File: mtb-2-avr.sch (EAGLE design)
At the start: 15 parts, among them IC1 MEGA328P-AU, Q1 14.745 MHz

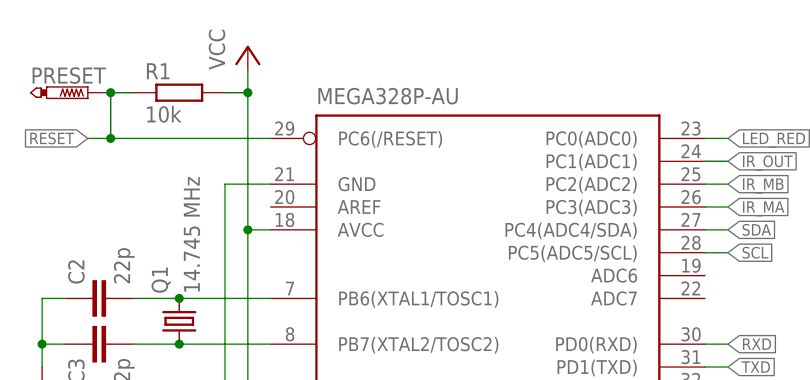
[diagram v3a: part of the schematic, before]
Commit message: Use ATmega8A, fix silksreen.
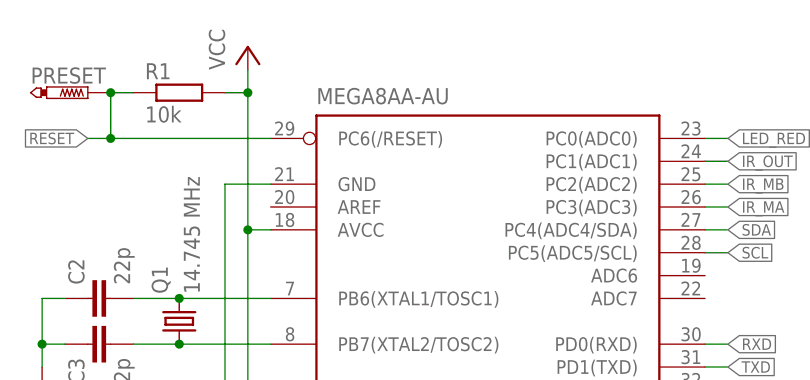
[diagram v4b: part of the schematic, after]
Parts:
- IC1: value MEGA328P-AU -> MEGA8AA-AU; LCSC_PART C14877 -> C16190
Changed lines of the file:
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@@
 <grid distance="0.1" unitdist="inch" unit="mm" style="lines" multiple="1" display="no" altdistance="0.01" altunitdist="inch" altunit="mm"/>
 <layers>
-<layer number="1" name="Top" color="3" fill="1" visible="yes" active="no"/>
-<layer number="2" name="Route2" color="16" fill="1" visible="yes" active="no"/>
-<layer number="3" name="Route3" color="17" fill="1" visible="yes" active="no"/>
-<layer number="4" name="Route4" color="18" fill="1" visible="yes" active="no"/>
-<layer number="5" name="Route5" color="19" fill="1" visible="yes" active="no"/>
-<layer number="6" name="Route6" color="25" fill="1" visible="yes" active="no"/>
-<layer number="7" name="Route7" color="26" fill="1" visible="yes" active="no"/>
-<layer number="8" name="Route8" color="27" fill="1" visible="yes" active="no"/>
-<layer number="9" name="Route9" color="28" fill="1" visible="yes" active="no"/>
-<layer number="10" name="Route10" color="29" fill="1" visible="yes" active="no"/>
-<layer number="11" name="Route11" color="30" fill="1" visible="yes" active="no"/>
-<layer number="12" name="Route12" color="20" fill="1" visible="yes" active="no"/>
-<layer number="13" name="Route13" color="21" fill="1" visible="yes" active="no"/>
-<layer number="14" name="Route14" color="22" fill="1" visible="yes" active="no"/>
-<layer number="15" name="Route15" color="23" fill="1" visible="yes" active="no"/>
-<layer number="16" name="Bottom" color="4" fill="1" visible="yes" active="no"/>
-<layer number="17" name="Pads" color="2" fill="1" visible="yes" active="no"/>
-<layer number="18" name="Vias" color="2" fill="1" visible="yes" active="no"/>
-<layer number="19" name="Unrouted" color="6" fill="1" visible="yes" active="no"/>
-<layer number="20" name="Dimension" color="24" fill="1" visible="yes" active="no"/>
-<layer number="21" name="tPlace" color="7" fill="1" visible="yes" active="no"/>
-<layer number="22" name="bPlace" color="7" fill="1" visible="yes" active="no"/>
-<layer number="23" name="tOrigins" color="15" fill="1" visible="yes" active="no"/>
-<layer number="24" name="bOrigins" color="15" fill="1" visible="yes" active="no"/>
-<layer number="25" name="tNames" color="7" fill="1" visible="yes" active="no"/>
-<layer number="26" name="bNames" color="7" fill="1" visible="yes" active="no"/>
-<layer number="27" name="tValues" color="7" fill="1" visible="yes" active="no"/>
-<layer number="28" name="bValues" color="7" fill="1" visible="yes" active="no"/>
+<layer number="1" name="Top" color="3" fill="1" visible="no" active="no"/>
+<layer number="2" name="Route2" color="16" fill="1" visible="no" active="no"/>
+<layer number="3" name="Route3" color="17" fill="1" visible="no" active="no"/>
+<layer number="4" name="Route4" color="18" fill="1" visible="no" active="no"/>
+<layer number="5" name="Route5" color="19" fill="1" visible="no" active="no"/>
+<layer number="6" name="Route6" color="25" fill="1" visible="no" active="no"/>
+<layer number="7" name="Route7" color="26" fill="1" visible="no" active="no"/>
+<layer number="8" name="Route8" color="27" fill="1" visible="no" active="no"/>
+<layer number="9" name="Route9" color="28" fill="1" visible="no" active="no"/>
+<layer number="10" name="Route10" color="29" fill="1" visible="no" active="no"/>
+<layer number="11" name="Route11" color="30" fill="1" visible="no" active="no"/>
+<layer number="12" name="Route12" color="20" fill="1" visible="no" active="no"/>
+<layer number="13" name="Route13" color="21" fill="1" visible="no" active="no"/>
+<layer number="14" name="Route14" color="22" fill="1" visible="no" active="no"/>
+<layer number="15" name="Route15" color="23" fill="1" visible="no" active="no"/>
+<layer number="16" name="Bottom" color="4" fill="1" visible="no" active="no"/>
+<layer number="17" name="Pads" color="2" fill="1" visible="no" active="no"/>
+<layer number="18" name="Vias" color="2" fill="1" visible="no" active="no"/>
+<layer number="19" name="Unrouted" color="6" fill="1" visible="no" active="no"/>
+<layer number="20" name="Dimension" color="24" fill="1" visible="no" active="no"/>
+<layer number="21" name="tPlace" color="7" fill="1" visible="no" active="no"/>
+<layer number="22" name="bPlace" color="7" fill="1" visible="no" active="no"/>
+<layer number="23" name="tOrigins" color="15" fill="1" visible="no" active="no"/>
+<layer number="24" name="bOrigins" color="15" fill="1" visible="no" active="no"/>
+<layer number="25" name="tNames" color="7" fill="1" visible="no" active="no"/>
+<layer number="26" name="bNames" color="7" fill="1" visible="no" active="no"/>
+<layer number="27" name="tValues" color="7" fill="1" visible="no" active="no"/>
+<layer number="28" name="bValues" color="7" fill="1" visible="no" active="no"/>
 <layer number="29" name="tStop" color="7" fill="3" visible="no" active="no"/>
 <layer number="30" name="bStop" color="7" fill="6" visible="no" active="no"/>
@@
 <layer number="35" name="tGlue" color="7" fill="4" visible="no" active="no"/>
 <layer number="36" name="bGlue" color="7" fill="5" visible="no" active="no"/>
-<layer number="37" name="tTest" color="7" fill="1" visible="yes" active="no"/>
-<layer number="38" name="bTest" color="7" fill="1" visible="yes" active="no"/>
+<layer number="37" name="tTest" color="7" fill="1" visible="no" active="no"/>
+<layer number="38" name="bTest" color="7" fill="1" visible="no" active="no"/>
 <layer number="39" name="tKeepout" color="4" fill="11" visible="no" active="no"/>
 <layer number="40" name="bKeepout" color="1" fill="11" visible="no" active="no"/>
@@
 <layer number="44" name="Drills" color="7" fill="1" visible="no" active="no"/>
 <layer number="45" name="Holes" color="7" fill="1" visible="no" active="no"/>
-<layer number="46" name="Milling" color="3" fill="1" visible="yes" active="no"/>
-<layer number="47" name="Measures" color="7" fill="1" visible="yes" active="no"/>
-<layer number="48" name="Document" color="7" fill="1" visible="yes" active="no"/>
-<layer number="49" name="Reference" color="7" fill="1" visible="yes" active="no"/>
-<layer number="50" name="dxf" color="7" fill="1" visible="yes" active="no"/>
-<layer number="51" name="tDocu" color="7" fill="1" visible="yes" active="no"/>
-<layer number="52" name="bDocu" color="7" fill="1" visible="yes" active="no"/>
-<layer number="53" name="tGND_GNDA" color="7" fill="9" visible="yes" active="no"/>
-<layer number="54" name="bGND_GNDA" color="1" fill="9" visible="yes" active="no"/>
-<layer number="56" name="wert" color="7" fill="1" visible="yes" active="no"/>
-<layer number="57" name="tCAD" color="7" fill="1" visible="yes" active="no"/>
-<layer number="59" name="tCarbon" color="7" fill="1" visible="yes" active="no"/>
-<layer number="60" name="bCarbon" color="7" fill="1" visible="yes" active="no"/>
+<layer number="46" name="Milling" color="3" fill="1" visible="no" active="no"/>
+<layer number="47" name="Measures" color="7" fill="1" visible="no" active="no"/>
+<layer number="48" name="Document" color="7" fill="1" visible="no" active="no"/>
+<layer number="49" name="Reference" color="7" fill="1" visible="no" active="no"/>
+<layer number="50" name="dxf" color="7" fill="1" visible="no" active="no"/>
+<layer number="51" name="tDocu" color="7" fill="1" visible="no" active="no"/>
+<layer number="52" name="bDocu" color="7" fill="1" visible="no" active="no"/>
+<layer number="53" name="tGND_GNDA" color="7" fill="9" visible="no" active="no"/>
+<layer number="54" name="bGND_GNDA" color="1" fill="9" visible="no" active="no"/>
+<layer number="56" name="wert" color="7" fill="1" visible="no" active="no"/>
+<layer number="57" name="tCAD" color="7" fill="1" visible="no" active="no"/>
+<layer number="59" name="tCarbon" color="7" fill="1" visible="no" active="no"/>
+<layer number="60" name="bCarbon" color="7" fill="1" visible="no" active="no"/>
 <layer number="88" name="SimResults" color="9" fill="1" visible="yes" active="yes"/>
 <layer number="89" name="SimProbes" color="9" fill="1" visible="yes" active="yes"/>
@@
 <part name="P+1" library="supply1" library_urn="urn:adsk.eagle:library:371" deviceset="VCC" device=""/>
 <part name="GND1" library="supply1" library_urn="urn:adsk.eagle:library:371" deviceset="GND" device=""/>
-<part name="IC1" library="atmel" library_urn="urn:adsk.eagle:library:105" deviceset="MEGA8" device="-AI" package3d_urn="urn:adsk.eagle:package:4313/2" value="MEGA328P-AU">
-<attribute name="LCSC_PART" value="C14877"/>
+<part name="IC1" library="atmel" library_urn="urn:adsk.eagle:library:105" deviceset="MEGA8" device="-AI" package3d_urn="urn:adsk.eagle:package:4313/2" value="MEGA8AA-AU">
+<attribute name="LCSC_PART" value="C16190"/>
 </part>
 <part name="C1" library="rcl" deviceset="C-EU" device="C0603" value="100n">

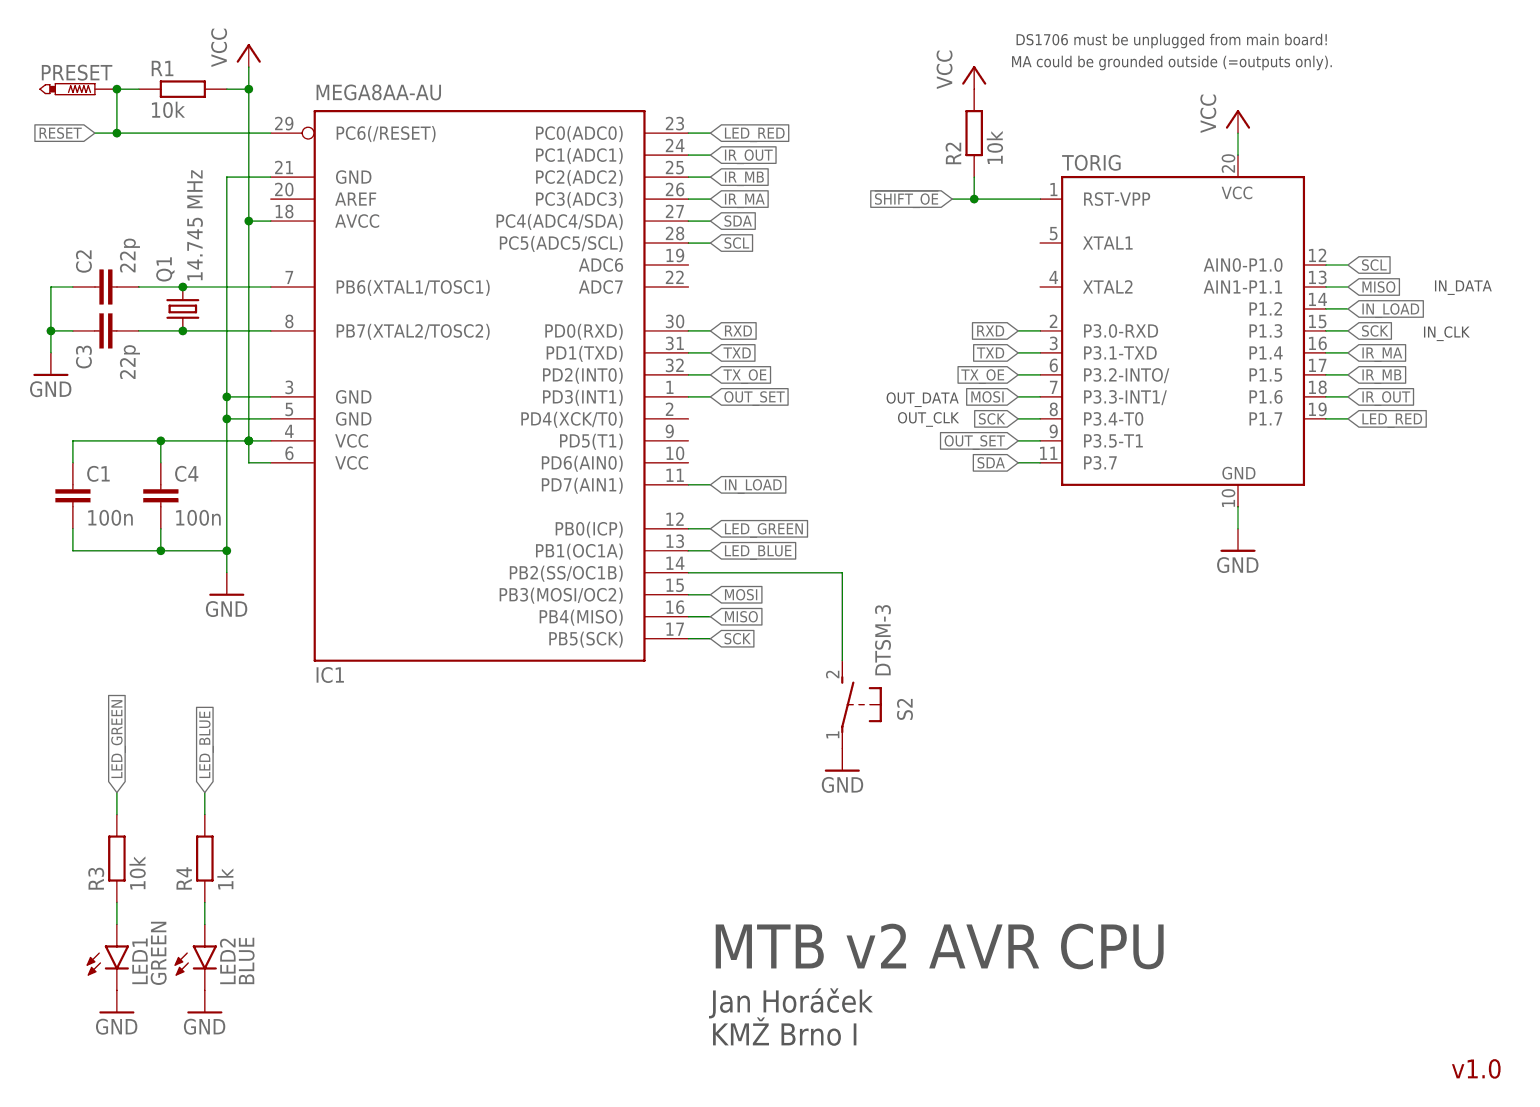
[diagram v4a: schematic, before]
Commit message: Silkscreen tweaks.
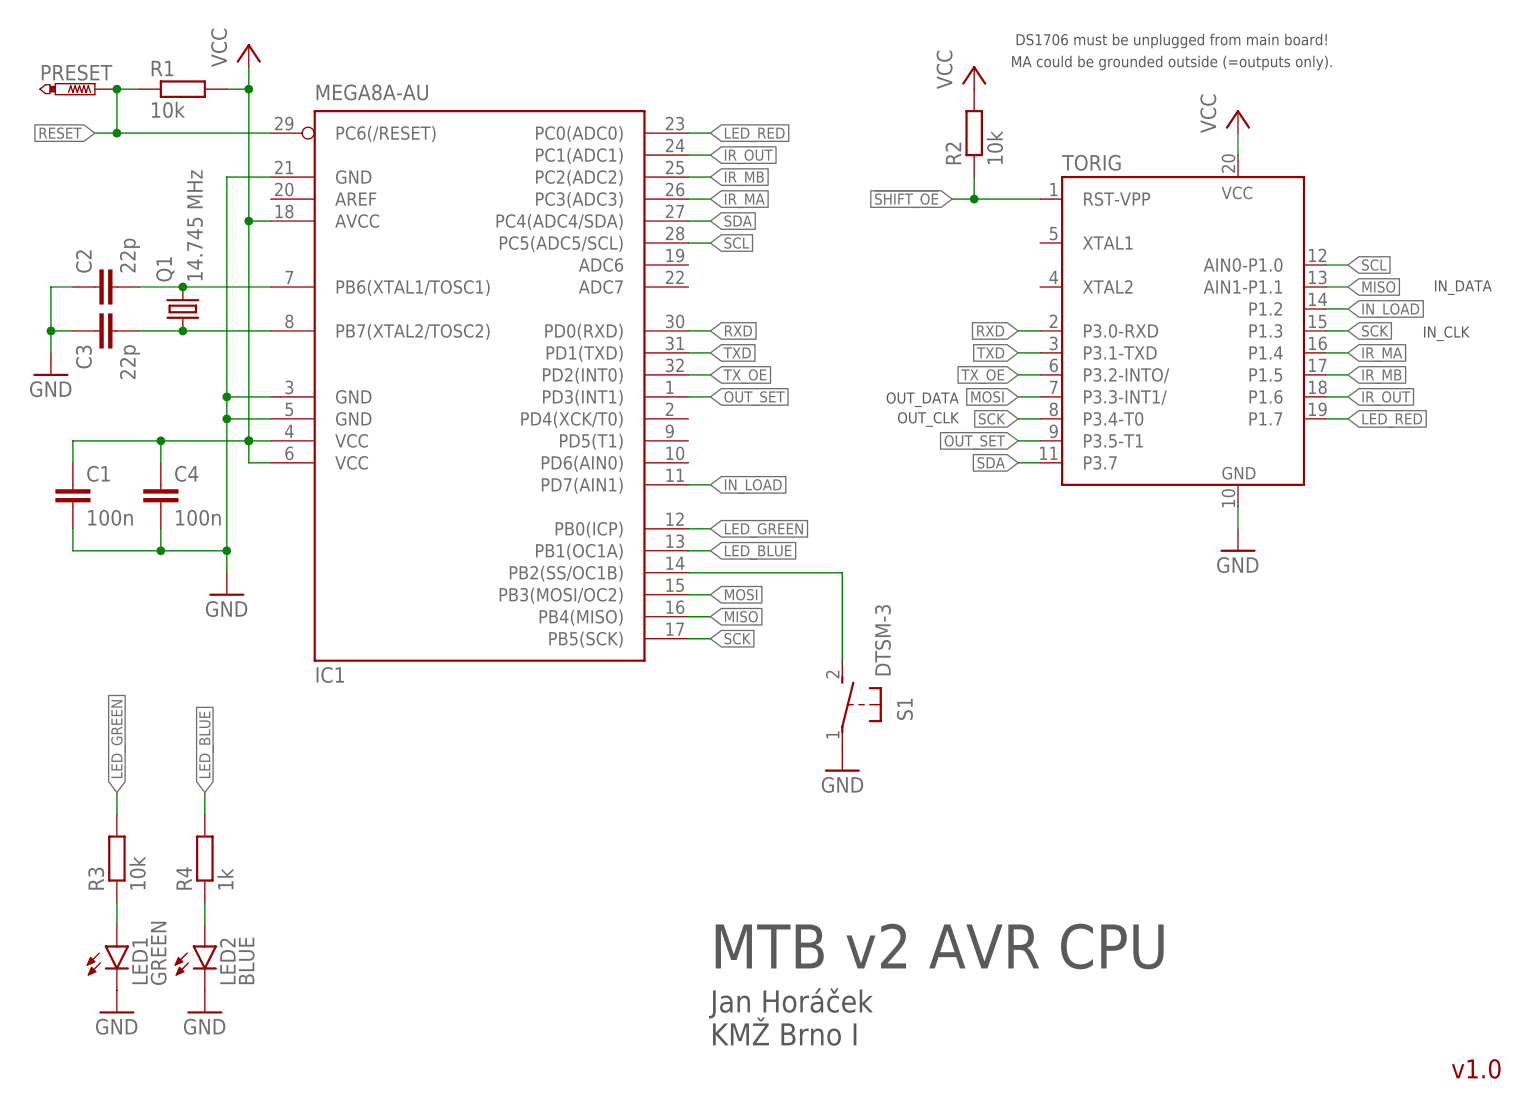
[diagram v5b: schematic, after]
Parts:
- IC1: value MEGA8AA-AU -> MEGA8A-AU
- renumbered S2 to S1
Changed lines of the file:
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@@
 <part name="P+1" library="supply1" library_urn="urn:adsk.eagle:library:371" deviceset="VCC" device=""/>
 <part name="GND1" library="supply1" library_urn="urn:adsk.eagle:library:371" deviceset="GND" device=""/>
-<part name="IC1" library="atmel" library_urn="urn:adsk.eagle:library:105" deviceset="MEGA8" device="-AI" package3d_urn="urn:adsk.eagle:package:4313/2" value="MEGA8AA-AU">
+<part name="IC1" library="atmel" library_urn="urn:adsk.eagle:library:105" deviceset="MEGA8" device="-AI" package3d_urn="urn:adsk.eagle:package:4313/2" value="MEGA8A-AU">
 <attribute name="LCSC_PART" value="C16190"/>
 </part>
@@
 </part>
 <part name="PRESET" library="testpad" library_urn="urn:adsk.eagle:library:385" deviceset="PTR1" device="B1,27" package3d_urn="urn:adsk.eagle:package:27944/2"/>
-<part name="S2" library="switch-tact" deviceset="DTSM-3" device=""/>
+<part name="S1" library="switch-tact" deviceset="DTSM-3" device=""/>
 <part name="GND4" library="supply1" library_urn="urn:adsk.eagle:library:371" deviceset="GND" device=""/>
 </parts>
@@
 <attribute name="TP_SIGNAL_NAME" x="12.7" y="118.11" size="1.778" layer="97" rot="R270"/>
 </instance>
-<instance part="S2" gate="G$1" x="101.6" y="48.26" smashed="yes" rot="MR0">
+<instance part="S1" gate="G$1" x="101.6" y="48.26" smashed="yes" rot="MR0">
 <attribute name="NAME" x="107.95" y="46.355" size="1.778" layer="95" rot="MR90"/>
 <attribute name="VALUE" x="105.41" y="51.435" size="1.778" layer="96" rot="MR90"/>
@@
 </segment>
 <segment>
-<pinref part="S2" gate="G$1" pin="1"/>
+<pinref part="S1" gate="G$1" pin="1"/>
 <pinref part="GND4" gate="1" pin="GND"/>
 </segment>
@@
 <net name="N$5" class="0">
 <segment>
-<pinref part="S2" gate="G$1" pin="2"/>
+<pinref part="S1" gate="G$1" pin="2"/>
 <pinref part="IC1" gate="G$1" pin="PB2(SS/OC1B)"/>
 <wire x1="101.6" y1="63.5" x2="101.6" y2="53.34" width="0.1524" layer="91"/>

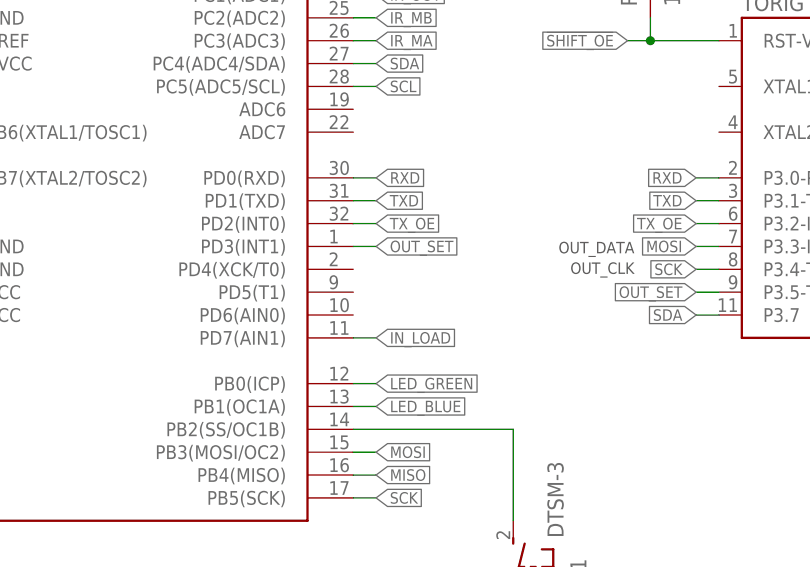
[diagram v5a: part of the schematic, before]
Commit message: Add test pad.
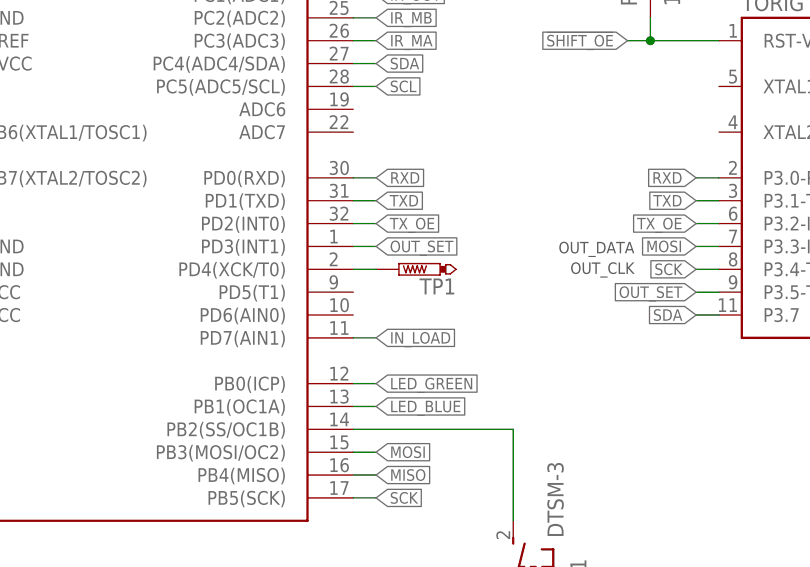
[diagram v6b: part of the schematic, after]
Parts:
- added TP1: PTR1B1,27, testpad:PTR1B1,27
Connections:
- new net TEST1: IC1.PD4(XCK/T0), TP1.TP
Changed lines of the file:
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@@
 <part name="S1" library="switch-tact" deviceset="DTSM-3" device=""/>
 <part name="GND4" library="supply1" library_urn="urn:adsk.eagle:library:371" deviceset="GND" device=""/>
+<part name="TP1" library="testpad" library_urn="urn:adsk.eagle:library:385" deviceset="PTR1" device="B1,27" package3d_urn="urn:adsk.eagle:package:27944/2"/>
 </parts>
 <sheets>
@@
 <instance part="GND4" gate="1" x="101.6" y="40.64" smashed="yes" rot="MR0">
 <attribute name="VALUE" x="104.14" y="38.1" size="1.778" layer="96" rot="MR0"/>
+</instance>
+<instance part="TP1" gate="G$1" x="88.9" y="81.28" smashed="yes" rot="R90">
+<attribute name="NAME" x="95.25" y="80.264" size="1.778" layer="95" rot="R180"/>
+<attribute name="TP_SIGNAL_NAME" x="91.44" y="82.55" size="1.778" layer="97" rot="R90"/>
 </instance>
 </instances>
@@
 </segment>
 </net>
+<net name="TEST1" class="0">
+<segment>
+<pinref part="IC1" gate="G$1" pin="PD4(XCK/T0)"/>
+<pinref part="TP1" gate="G$1" pin="TP"/>
+<wire x1="86.36" y1="81.28" x2="83.82" y2="81.28" width="0.1524" layer="91"/>
+</segment>
+</net>
